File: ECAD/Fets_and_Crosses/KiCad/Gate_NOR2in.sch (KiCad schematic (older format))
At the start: 4 parts, among them Q493 2N7002, Q494 BSS84, Q495 BSS84, Q496 2N7002

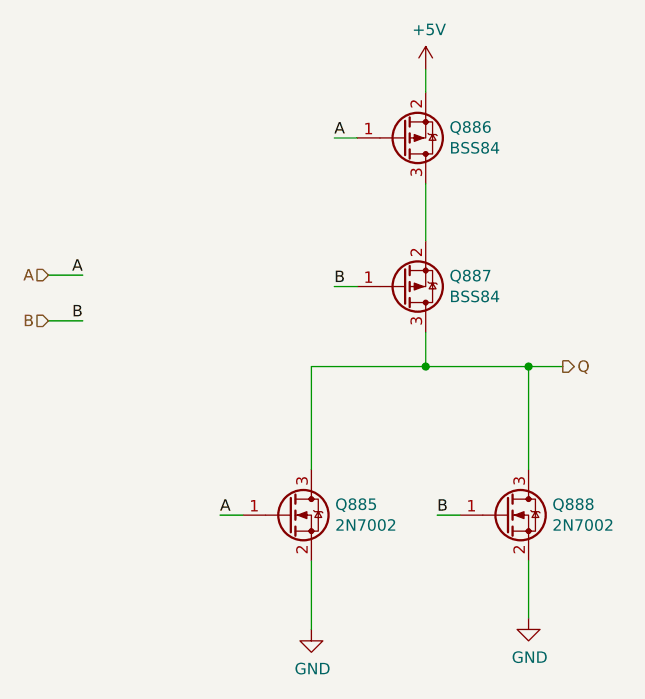
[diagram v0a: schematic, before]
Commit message: POR, Tooling Holes
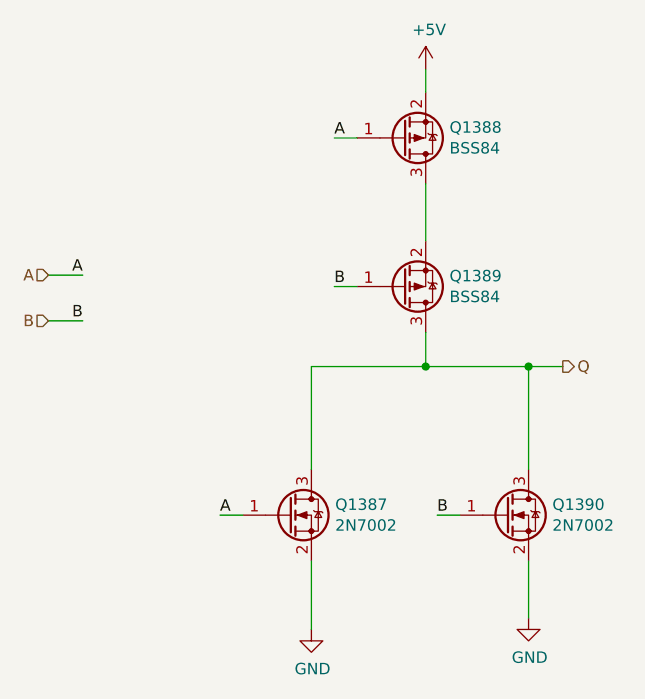
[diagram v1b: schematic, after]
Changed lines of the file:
@@
 $Descr A4 11693 8268
 encoding utf-8
-Sheet 244 362
+Sheet 244 363
 Title "Fets and Crosses"
 Date "2021-05-23"
@@
 AR Path="/5FB775FE/5F1827D4/5F172B07/5E56263B/5E557A8F" Ref="Q1319"  Part="1"
 AR Path="/5E553405/5F22E6FE/5E56263B/5E557A8F" Ref="Q659"  Part="1"
-F 0 "Q887" H 5304 2454 50  0000 L CNN
+AR Path="/5E53AD22/5E6A228F/620124C2/5E56263B/5E557A8F" Ref="Q1389"  Part="1"
+F 0 "Q1389" H 5304 2454 50  0000 L CNN
 F 1 "BSS84" H 5304 2545 50  0000 L CNN
 F 2 "LogicQ:SOT-23-P" H 5300 2600 50  0001 C CNN
@@
 AR Path="/5FB775FE/5F1827D4/5F172B07/5E56263B/5E557A95" Ref="Q1317"  Part="1"
 AR Path="/5E553405/5F22E6FE/5E56263B/5E557A95" Ref="Q657"  Part="1"
-F 0 "Q885" H 4804 3546 50  0000 L CNN
+AR Path="/5E53AD22/5E6A228F/620124C2/5E56263B/5E557A95" Ref="Q1387"  Part="1"
+F 0 "Q1387" H 4804 3546 50  0000 L CNN
 F 1 "2N7002" H 4804 3455 50  0000 L CNN
 F 2 "LogicQ:SOT-23-N" H 4800 3600 50  0001 C CNN
@@
 AR Path="/5FB775FE/5F1827D4/5F172B07/5E56263B/5E557A9B" Ref="Q1318"  Part="1"
 AR Path="/5E553405/5F22E6FE/5E56263B/5E557A9B" Ref="Q658"  Part="1"
-F 0 "Q886" H 5304 1804 50  0000 L CNN
+AR Path="/5E53AD22/5E6A228F/620124C2/5E56263B/5E557A9B" Ref="Q1388"  Part="1"
+F 0 "Q1388" H 5304 1804 50  0000 L CNN
 F 1 "BSS84" H 5304 1895 50  0000 L CNN
 F 2 "LogicQ:SOT-23-P" H 5300 1950 50  0001 C CNN
@@
 AR Path="/5FB775FE/5F1827D4/5F172B07/5E56263B/5E557AAE" Ref="#PWR0930"  Part="1"
 AR Path="/5E553405/5F22E6FE/5E56263B/5E557AAE" Ref="#PWR0494"  Part="1"
+AR Path="/5E53AD22/5E6A228F/620124C2/5E56263B/5E557AAE" Ref="#PWR07"  Part="1"
 F 0 "#PWR0653" H 5650 3700 50  0001 C CNN
 F 1 "GND" H 5655 3777 50  0000 C CNN
@@
 AR Path="/5FB775FE/5F1827D4/5F172B07/5E56263B/5E557ABB" Ref="#PWR0931"  Part="1"
 AR Path="/5E553405/5F22E6FE/5E56263B/5E557ABB" Ref="#PWR0495"  Part="1"
+AR Path="/5E53AD22/5E6A228F/620124C2/5E56263B/5E557ABB" Ref="#PWR06"  Part="1"
 F 0 "#PWR0654" H 5200 1400 50  0001 C CNN
 F 1 "+5V" H 5215 1723 50  0000 C CNN
@@
 AR Path="/5FB775FE/5F1827D4/5F172B07/5E56263B/5E557AA1" Ref="Q1320"  Part="1"
 AR Path="/5E553405/5F22E6FE/5E56263B/5E557AA1" Ref="Q660"  Part="1"
-F 0 "Q888" H 5754 3546 50  0000 L CNN
+AR Path="/5E53AD22/5E6A228F/620124C2/5E56263B/5E557AA1" Ref="Q1390"  Part="1"
+F 0 "Q1390" H 5754 3546 50  0000 L CNN
 F 1 "2N7002" H 5754 3455 50  0000 L CNN
 F 2 "LogicQ:SOT-23-N" H 5750 3600 50  0001 C CNN
@@
 AR Path="/5FB775FE/5F1827D4/5F172B07/5E56263B/5E559196" Ref="#PWR0932"  Part="1"
 AR Path="/5E553405/5F22E6FE/5E56263B/5E559196" Ref="#PWR0496"  Part="1"
+AR Path="/5E53AD22/5E6A228F/620124C2/5E56263B/5E559196" Ref="#PWR05"  Part="1"
 F 0 "#PWR0655" H 4700 3750 50  0001 C CNN
 F 1 "GND" H 4705 3827 50  0000 C CNN

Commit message: Seperated Red/Green LEDs
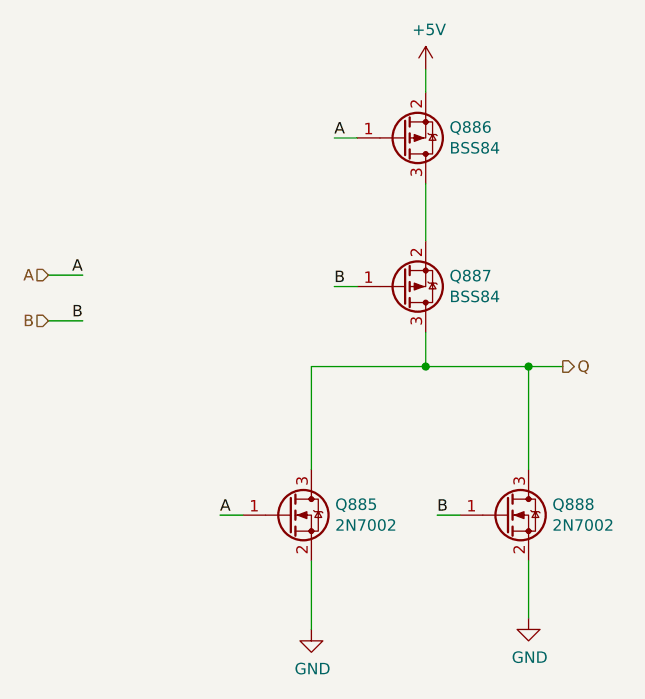
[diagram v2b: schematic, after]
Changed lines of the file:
@@
 AR Path="/5E553405/5F22E6FE/5E56263B/5E557A8F" Ref="Q659"  Part="1"
 AR Path="/5E53AD22/5E6A228F/620124C2/5E56263B/5E557A8F" Ref="Q1389"  Part="1"
-F 0 "Q1389" H 5304 2454 50  0000 L CNN
+F 0 "Q887" H 5304 2454 50  0000 L CNN
 F 1 "BSS84" H 5304 2545 50  0000 L CNN
 F 2 "LogicQ:SOT-23-P" H 5300 2600 50  0001 C CNN
@@
 AR Path="/5E553405/5F22E6FE/5E56263B/5E557A95" Ref="Q657"  Part="1"
 AR Path="/5E53AD22/5E6A228F/620124C2/5E56263B/5E557A95" Ref="Q1387"  Part="1"
-F 0 "Q1387" H 4804 3546 50  0000 L CNN
+F 0 "Q885" H 4804 3546 50  0000 L CNN
 F 1 "2N7002" H 4804 3455 50  0000 L CNN
 F 2 "LogicQ:SOT-23-N" H 4800 3600 50  0001 C CNN
@@
 AR Path="/5E553405/5F22E6FE/5E56263B/5E557A9B" Ref="Q658"  Part="1"
 AR Path="/5E53AD22/5E6A228F/620124C2/5E56263B/5E557A9B" Ref="Q1388"  Part="1"
-F 0 "Q1388" H 5304 1804 50  0000 L CNN
+F 0 "Q886" H 5304 1804 50  0000 L CNN
 F 1 "BSS84" H 5304 1895 50  0000 L CNN
 F 2 "LogicQ:SOT-23-P" H 5300 1950 50  0001 C CNN
@@
 AR Path="/5E553405/5F22E6FE/5E56263B/5E557AA1" Ref="Q660"  Part="1"
 AR Path="/5E53AD22/5E6A228F/620124C2/5E56263B/5E557AA1" Ref="Q1390"  Part="1"
-F 0 "Q1390" H 5754 3546 50  0000 L CNN
+F 0 "Q888" H 5754 3546 50  0000 L CNN
 F 1 "2N7002" H 5754 3455 50  0000 L CNN
 F 2 "LogicQ:SOT-23-N" H 5750 3600 50  0001 C CNN

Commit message: Added Most LCSC Part Numbers
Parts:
- Q493, Q496: LCSC (none) -> C8545
- Q494, Q495: LCSC (none) -> C114481
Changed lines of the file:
@@
 F 2 "LogicQ:SOT-23-P" H 5300 2600 50  0001 C CNN
 F 3 "~" H 5100 2500 50  0001 C CNN
+F 4 "C114481" H 5100 2500 50  0001 C CNN "LCSC"
 	1    5100 2500
 	1    0    0    1
@@
 F 2 "LogicQ:SOT-23-N" H 4800 3600 50  0001 C CNN
 F 3 "~" H 4600 3500 50  0001 C CNN
+F 4 "C8545" H 4600 3500 50  0001 C CNN "LCSC"
 	1    4600 3500
 	1    0    0    -1
@@
 F 2 "LogicQ:SOT-23-P" H 5300 1950 50  0001 C CNN
 F 3 "~" H 5100 1850 50  0001 C CNN
+F 4 "C114481" H 5100 1850 50  0001 C CNN "LCSC"
 	1    5100 1850
 	1    0    0    1
@@
 F 2 "LogicQ:SOT-23-N" H 5750 3600 50  0001 C CNN
 F 3 "~" H 5550 3500 50  0001 C CNN
+F 4 "C8545" H 5550 3500 50  0001 C CNN "LCSC"
 	1    5550 3500
 	1    0    0    -1
